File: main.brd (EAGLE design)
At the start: 100 x 50 mm, 85 parts, among them IC1 PM8834-SO08N, IC17 LD398533RM, IC18 LD1117S50TR, IC2 PM8834-SO08N, Q1 IRF3205SPBF, Q2 IRF3205SPBF, Q3 IRF3205SPBF, Q4 IRF3205SPBF, Q5 BSS138, Q6 BSS138, Q7 BSS138, Q8 BSS138, U1 TMP275AIDR, U2 SI7021, U4 ESP-WROOM-32, X1 1751251, X2 1751248, X3 1751251, X4 1751277

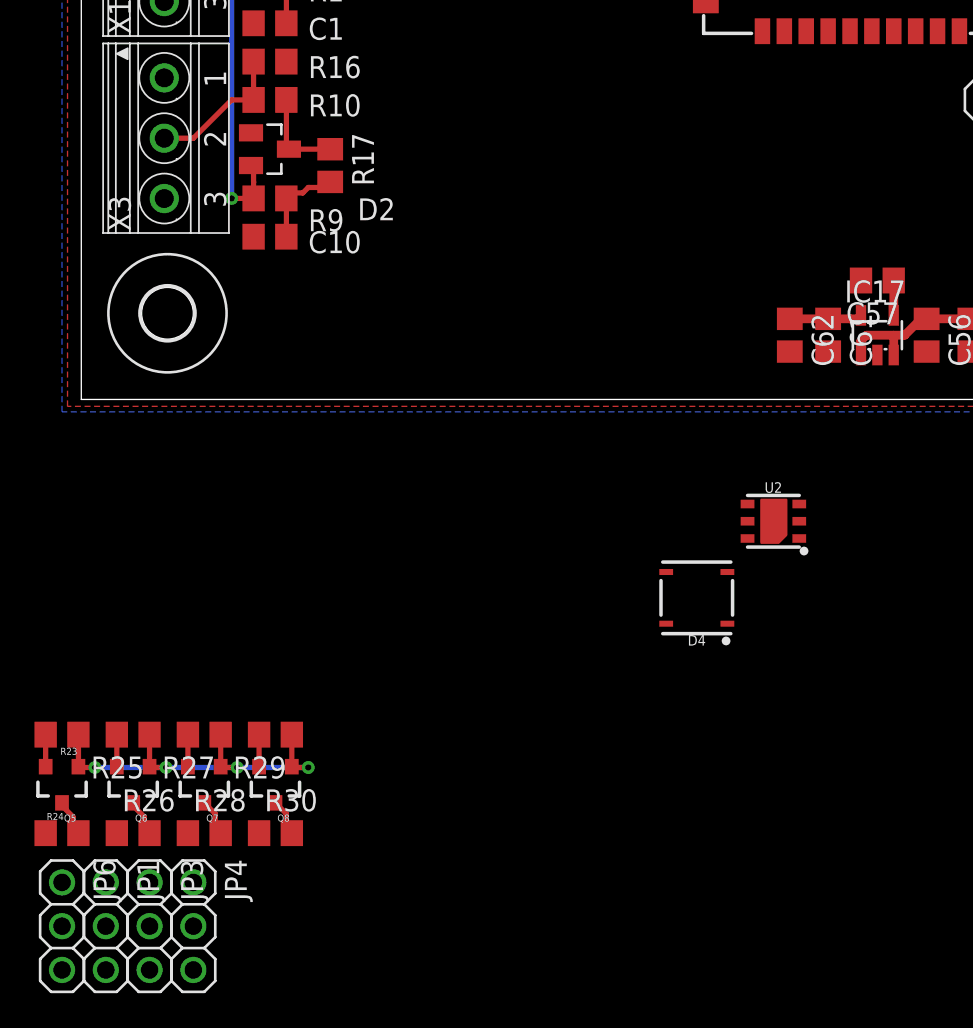
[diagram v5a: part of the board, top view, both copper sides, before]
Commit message: Removed sensors
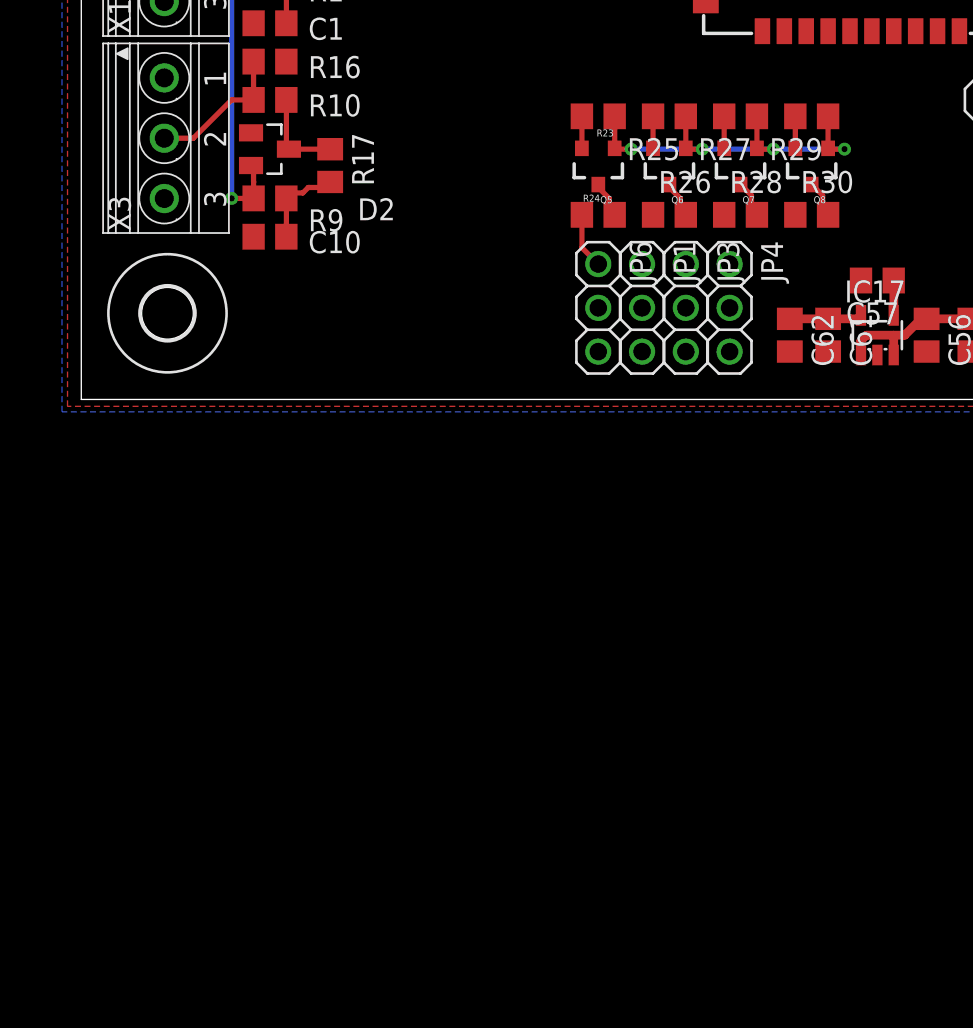
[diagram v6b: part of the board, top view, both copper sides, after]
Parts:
- removed D4: TSOP57238TT1, SparkFun-Sensors:TSOP572
- removed U2: SI7021, SparkFun-Sensors:DFN-6-3X3-SI7021
- moved JP1 47.5 mm to (-17.5, -19.7)
- moved JP3 47.5 mm to (-14.9, -19.7)
- moved JP4 47.5 mm to (-12.4, -19.7)
- moved Q6 47.5 mm to (-15.9, -11.4)
- moved R23 47.5 mm to (-20.0, -8.57)
- moved R25 47.5 mm to (-15.9, -8.57)
- moved R26 47.5 mm to (-15.9, -14.3)
- moved R27 47.5 mm to (-11.7, -8.57)
- moved R29 47.5 mm to (-7.62, -8.57)
- moved JP6 47.5 mm to (-20.0, -19.7)
- moved Q5 47.5 mm to (-20.0, -11.4)
- moved Q7 47.5 mm to (-11.7, -11.4)
- moved Q8 47.5 mm to (-7.62, -11.4)
- moved R24 47.5 mm to (-20.0, -14.3)
- moved R28 47.5 mm to (-11.7, -14.3)
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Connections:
- removed net VDD: U2.VDD
- net +5V: now also JP6.1, R24.1
- net GND: no longer U2.GND
- net HV: no longer JP6.1, R24.1
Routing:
- net +5V: track 5.67 -> 8.92 mm

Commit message: P1 port and layouting
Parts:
- removed D3: BAT60JFILM, diode:SOD323-W
- removed JP2: (no value), pinhead:1X04
- removed LED1: ROOD, led:CHIP-LED0805
- removed R6: 1K, resistor:R0805
- added C11: (no value), resistor:SMC_A
- added C13, C30: 100nF, resistor:C0805
- added C14: 100n, resistor:C0805
- added C28, C29: 12pF, resistor:C0805
- added CN2: (no value), adafruit:USB-MINIB
- added D4: BAT54S, diode:SOT23
- added D5: BAT60JFILM, diode:SOD323-W
- added IC4: CP2102, silabs:MLP28
- added J1: RJ11, SparkFun-Connectors:RJ11-6
- added JP5: (no value), pinhead:1X06
- added LED2: RGBLED5050, adafruit:RGBLED5050
- added Q10: (no value), crystal:TC38H
- added Q11, Q12, Q9: BSS138, SparkFun:SOT23-3
- added R31, R32: 0R, resistor:R0805
- added R33: 2K, resistor:R0805
- added R34, R40, R42, R43, R44, R45: 10K, resistor:R0805
- added R35: 22K1, resistor:R0805
- added R36: 47K5, resistor:R0805
- added R37, R38: (no value), resistor:R0805
- added R41: 1K, resistor:R0805
- added S3: MOMENTARY-SWITCH-SPST-SMD-5.2-REDUNDANT, SparkFun-Switches:TACTILE_SWITCH_SMD_5.2MM
- added T1, T2, T3: SS8050-G, transistor:SOT23-BEC
- moved D14 25.7 mm to (6.67, -46.0)
- moved C58 24.8 mm to (1.91, -46.0), turned to 180 degrees
- moved R23 24.5 mm to (-21.6, -33.0)
- moved R25 24.5 mm to (-17.5, -33.0)
- moved R27 24.5 mm to (-13.3, -33.0)
- moved R29 24.5 mm to (-9.21, -33.0)
- moved JP1 24.5 mm to (-19.1, -44.1)
- moved JP3 24.5 mm to (-16.5, -44.1)
- moved JP4 24.5 mm to (-14.0, -44.1)
- moved JP6 24.5 mm to (-21.6, -44.1)
- moved Q5 24.5 mm to (-21.6, -35.9)
- moved Q6 24.5 mm to (-17.5, -35.9)
- moved Q7 24.5 mm to (-13.3, -35.9)
- moved Q8 24.5 mm to (-9.21, -35.9)
- moved R24 24.5 mm to (-21.6, -38.7)
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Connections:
- removed net N$113: C56.1, C58.1, D14.C, D3.C, IC17.1, IC17.3
- removed net N$5: LED1.A, R6.1
- removed net RDX0: JP2.4, U4.34
- removed net UART_5V: D3.A, JP2.1
- new net CTS: IC4.23, JP5.6
- new net DCD: IC4.1
- new net DSR: IC4.27
- new net DTR: IC4.28, R42.1, T2.E
- new net EN: C3.1, R7.1, T1.C, U4.3
- new net IO0: C30.1, S3.3, S3.4, T2.C, U4.25
- new net N$1: Q9.3, R40.2
- new net N$11: LED2.6, R44.1
- new net N$19: IC4.11, R34.1
- new net N$21: IC4.9, R33.1
- new net N$23: C60.+, D14.A, IC18.4, R39.2
- new net N$24: IC4.8, R35.2, R36.2
- new net N$25: CN2.D-, IC4.5
- new net N$26: J1.5, R37.1, R38.1
- new net N$27: C14.1, D4.3, R38.2, T3.B
- new net N$28: R41.1, T3.C
- new net N$29: LED2.4, R45.1
- new net N$30: LED2.5, R40.1
- new net N$31: Q11.3, R44.2
- new net N$32: Q12.3, R45.2
- new net N$37: Q12.1
- new net N$38: C28.1, Q10.2, U4.8
- new net N$39: C29.1, Q10.1, U4.9
- new net N$40: Q11.1
- new net N$41: Q9.1
- new net N$42: R42.2, T1.B
- new net N$43: R43.2, T2.B
- new net RI: IC4.2
- new net RTS: IC4.24, JP5.5, R43.1, T1.E
- new net RXD: IC4.25, JP5.3, R32.1
- new net RXD0: R31.2, U4.34
- new net TXD: IC4.26, JP5.4, R31.1
- new net VBUS: CN2.VBUS, D5.A, JP5.1, R35.1
- net +3V3: now also C11.+, C13.1, IC4.6, IC4.7, LED2.1, LED2.2, LED2.3, R33.2, R41.2
- net +5V: now also C56.1, C58.1, D14.C, D4.2, D5.C, IC17.1, IC17.3, J1.2, R37.2; no longer C60.+, D14.A, IC18.4, R39.2
- net BTN: now also S1.1; no longer S1.2
- net GND: now also C11.-, C13.2, C14.2, C28.2, C29.2, C30.2, CN2.GND, D4.1, IC4.3, IC4.EXP, IC4.M, J1.3, JP5.2, Q11.2, Q12.2, Q9.2, R34.2, R36.1, S3.1, S3.2, T3.E; no longer JP2.2, LED1.C
- net INP1: now also U4.11; no longer U4.10
- net INP2: now also U4.10; no longer U4.9
- net LED: now also U4.12; no longer R6.2, U4.8
- net N$6: now also CN2.D+, IC4.4; no longer C3.1, R7.1, U4.3
- net TXD0: now also R32.2; no longer JP2.3
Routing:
- net N$23: track 0.00 -> 31.9 mm, vias 0 -> 1
- net IO0: track 0.00 -> 29.6 mm, vias 0 -> 3
- net RXD0: track 0.00 -> 21.7 mm, vias 0 -> 2
- net DTR: track 0.00 -> 20.0 mm, vias 0 -> 2
- net RDX0: track 18.5 -> 0.00 mm, vias 1 -> 0
- net BTN: track 17.6 -> 2.23 mm, vias 2 -> 0
- net EN: track 0.00 -> 15.0 mm, vias 0 -> 1
- net N$25: track 0.00 -> 10.7 mm, vias 0 -> 2
- net N$24: track 0.00 -> 10.7 mm, vias 0 -> 2
- net N$113: track 8.86 -> 0.00 mm
- net +5V: track 8.92 -> 17.0 mm
- net RTS: track 0.00 -> 7.60 mm
- net N$42: track 0.00 -> 7.20 mm
- net +3V3: track 78.5 -> 85.3 mm
- net N$43: track 0.00 -> 5.51 mm, vias 0 -> 2
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
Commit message: Updatesss
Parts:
- removed C7, C9: 100n, resistor:C0805
- removed JP5: (no value), pinhead:1X06
- removed T3: SS8050-G, transistor:SOT23-BEC
- removed X1, X3: 1751251, con-phoenix-350:1751251
- added C15: 100n, resistor:C0805
- added D3: BAT54S, diode:SOT23
- added Q13: BSS138, SparkFun:SOT23-3
- added R46: 10R, resistor:R0805
- added R47: X, resistor:R0805
- added R48: 1K, resistor:R0805
- added R6: 10K, resistor:R0805
- added X5: 1751280, con-phoenix-350:1751280
- C6, C8: value 10nF X7R -> 1uF X7R
- R37: value (none) -> 10K
- R38: value (none) -> 1K
- R41: value 1K -> 10K
- moved R29 40.3 mm to (-31.4, -66.7), turned to 90 degrees
- moved Q8 39.7 mm to (-34.3, -66.7), turned to 90 degrees
- moved R30 39.5 mm to (-37.1, -66.7), turned to 270 degrees
- moved R27 34.6 mm to (-31.4, -62.5), turned to 90 degrees
- moved Q7 33.9 mm to (-34.3, -62.5), turned to 90 degrees
- moved R28 33.7 mm to (-37.1, -62.5), turned to 270 degrees
- moved JP4 33.7 mm to (-42.5, -61.9), turned to 180 degrees
- moved LED14 32.8 mm to (-14.6, -4.76)
- moved D4 32.6 mm to (-28.6, -5.40)
- moved R37 32.6 mm to (-28.6, -8.26)
- moved J1 32.5 mm to (-25.1, -20.0)
- moved C14 32.4 mm to (-24.4, -6.03), turned to 0 degrees
- moved R38 32.4 mm to (-24.4, -8.26)
- moved R41 32.3 mm to (-20.3, -4.45), turned to 0 degrees
- moved C57 32.1 mm to (-11.4, -13.0)
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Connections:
- new net N$33: D3.3, R46.2, R48.1
- new net N$5: R46.1, R47.2
- net +12V: now also R13.2, R14.2; no longer C7.1, C9.1
- net +3V3: now also D3.2, R6.2
- net CTS: no longer JP5.6
- net GND: now also C15.2, D3.1, Q13.2, R47.1, X5.3, X5.6; no longer C7.2, C9.2, JP5.2, R13.2, R14.2, T3.E, X1.3, X3.3
- net INP2: now also C15.1, R48.2, R6.1
- net N$10: now also IC1.4; no longer IC1.1
- net N$2: now also X5.5; no longer X1.2
- net N$20: now also X5.2; no longer X3.2
- net N$22: now also X5.1; no longer X3.1
- net N$27: now also Q13.1; no longer T3.B
- net N$28: now also Q13.3; no longer T3.C
- net N$4: now also X5.4; no longer X1.1
- net N$9: now also IC1.1; no longer IC1.4
- net RTS: no longer JP5.5
- net RXD: no longer JP5.3
- net TXD: no longer JP5.4
- net VBUS: no longer JP5.1
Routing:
- net EN: track 15.0 -> 48.9 mm, vias 1 -> 2
- net +3V3: track 85.3 -> 104.0 mm, vias 8 -> 9
- net +12V: track 67.4 -> 85.7 mm, vias 3 -> 5
- net +5V: track 17.0 -> 5.22 mm
- net N$23: track 31.9 -> 24.0 mm
- net N$27: track 0.00 -> 7.73 mm
- net N$13: track 14.3 -> 17.7 mm
- net N$12: track 5.86 -> 8.72 mm
- net N$102: track 2.48 -> 0.00 mm
- net N$28: track 0.00 -> 2.47 mm
- net N$26: track 0.00 -> 2.23 mm
- net TXD0: track 25.5 -> 27.0 mm
- net IO0: track 29.6 -> 31.1 mm
- net N$42: track 7.20 -> 5.78 mm
- net GND: track 2.15 -> 3.57 mm, vias 33 -> 39
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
